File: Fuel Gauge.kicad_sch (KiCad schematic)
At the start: 41 parts, among them Q15 BCX56, Q17 BSS84, Q20 BSS138, Q21 BSS123, Q22 ZXMP10A13F, SW3 DISPLAY, U3 BQ78350DBT-R1A, U4 TPD1E05U06DYA, U5 TPD1E05U06DYA

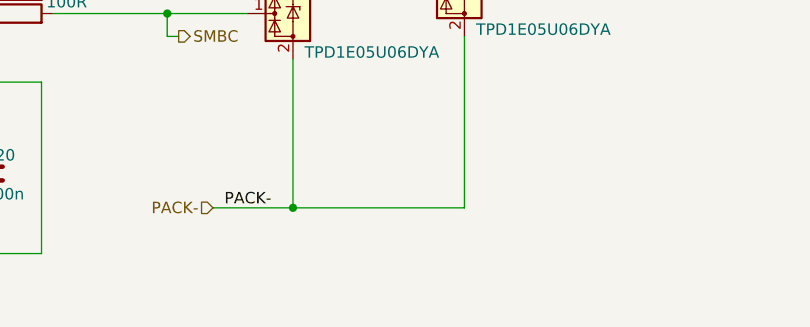
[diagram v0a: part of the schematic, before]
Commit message: forgot to give credit to TIDA-00792
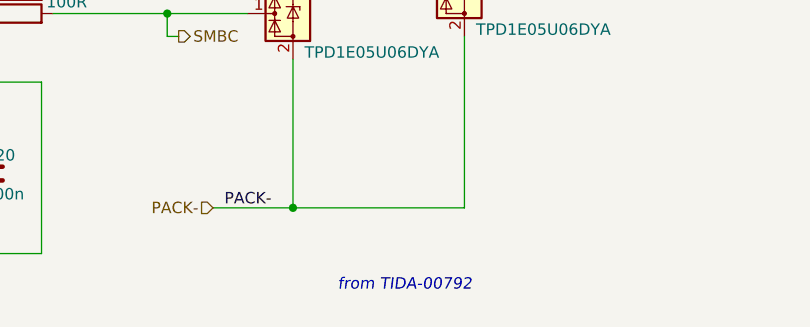
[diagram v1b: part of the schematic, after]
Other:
- note added: "from TIDA-00792"
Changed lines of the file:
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@@
+		)
+	)
+	(text "from TIDA-00792"
+		(exclude_from_sim no)
+		(at 197.866 129.286 0)
+		(effects
+			(font
+				(size 1.27 1.27)
+				(italic yes)
+			)
 		)
 	)

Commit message: ready to start first pass review on bms
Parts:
- removed C35: 3300p, symbol Device:C
- removed C36: 100n, symbol Device:C
- removed D30, D31, D32, D38: GREEN, PCM_Diode_SMD_AKL:D_0805_2012Metric, symbol PCM_SL_Devices:LED
- removed Q15: BCX56, Package_TO_SOT_SMD:SOT-89-3, symbol Transistor_BJT:BCX56
- removed Q17: BSS84, Package_TO_SOT_SMD:SOT-23, symbol Transistor_FET:BSS84
- removed Q20: BSS138, Package_TO_SOT_SMD:SOT-23, symbol Transistor_FET:BSS138
- removed R67, R68: 100k, symbol Device:R
- removed R69: 499k, symbol Device:R
- removed R70: 7k68, symbol Device:R
- removed R78: 220k, symbol Device:R
- removed R81: 1M, symbol Device:R
- removed SW3: DISPLAY, symbol Switch:SW_Push
- added C38: 100n, symbol Device:C
- added D34, D35, D36, D37: GREEN, PCM_Diode_SMD_AKL:D_0805_2012Metric, symbol PCM_SL_Devices:LED
- added Q20: BCX56, Package_TO_SOT_SMD:SOT-89-3, symbol Transistor_BJT:BCX56
- added R77: 100k, symbol Device:R
- R79: renamed from R82; value 220k -> 100k
- R80: renamed from R76; value 113k -> 100k
- renumbered C38 to C34, C39 to C35, C37 to C36, C20 to C37, D26 to D33, D33 to D38, Q22 to Q18, Q21 to Q19, R80 to R71, R83 to R72, R86 to R73, R85 to R74, R87 to R75, R84 to R76, R88 to R78, R75 to R81, R79 to R82, R89 to R83, R90 to R84, R53 to R85
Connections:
- net C8: now also Q20.2 (C)
- net CAP1: now also Q20.1 (B)
- net GND: now also U3.14 (~{DISP}), U3.8 (~{PRES}), U3.9 (~{KEYIN}), C38.2
- net at D33.2 (A), Q18.1 (G), R74.1: now also R77.1; no longer R79.1
- net LED1: no longer names the net of U3.16 (LED1)
- net LED1: now also D34.1
- net LED2: no longer names the net of U3.17 (LED2)
- net LED2: now also D35.1
- net LED3: no longer names the net of U3.18 (LED3)
- net LED3: now also D36.1
- net LED4: no longer names the net of U3.19 (LED4)
- net LED4: now also D37.1
- net LED5: no longer names the net of D38.1, U3.20 (LED5)
- net LEDP: no longer names the net of D38.2
- net LEDP: now also C38.1, D34.2, D35.2, D36.2, D37.2, Q20.3 (E)
- new net: R77.2, R79.1
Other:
- note removed: "***TODO: ~{KEYIN}***"
- note removed: "***TODO: ~{PRES}***"
- note removed: "from slua810"
- moved on the sheet: C34, C35, C36, C37, D33, D38, Q18, Q19, R71, R72, R73, R74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
